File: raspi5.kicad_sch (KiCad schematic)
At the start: 6 parts, among them J1 GPIO, J3 68711614522, U1 FT24C256A

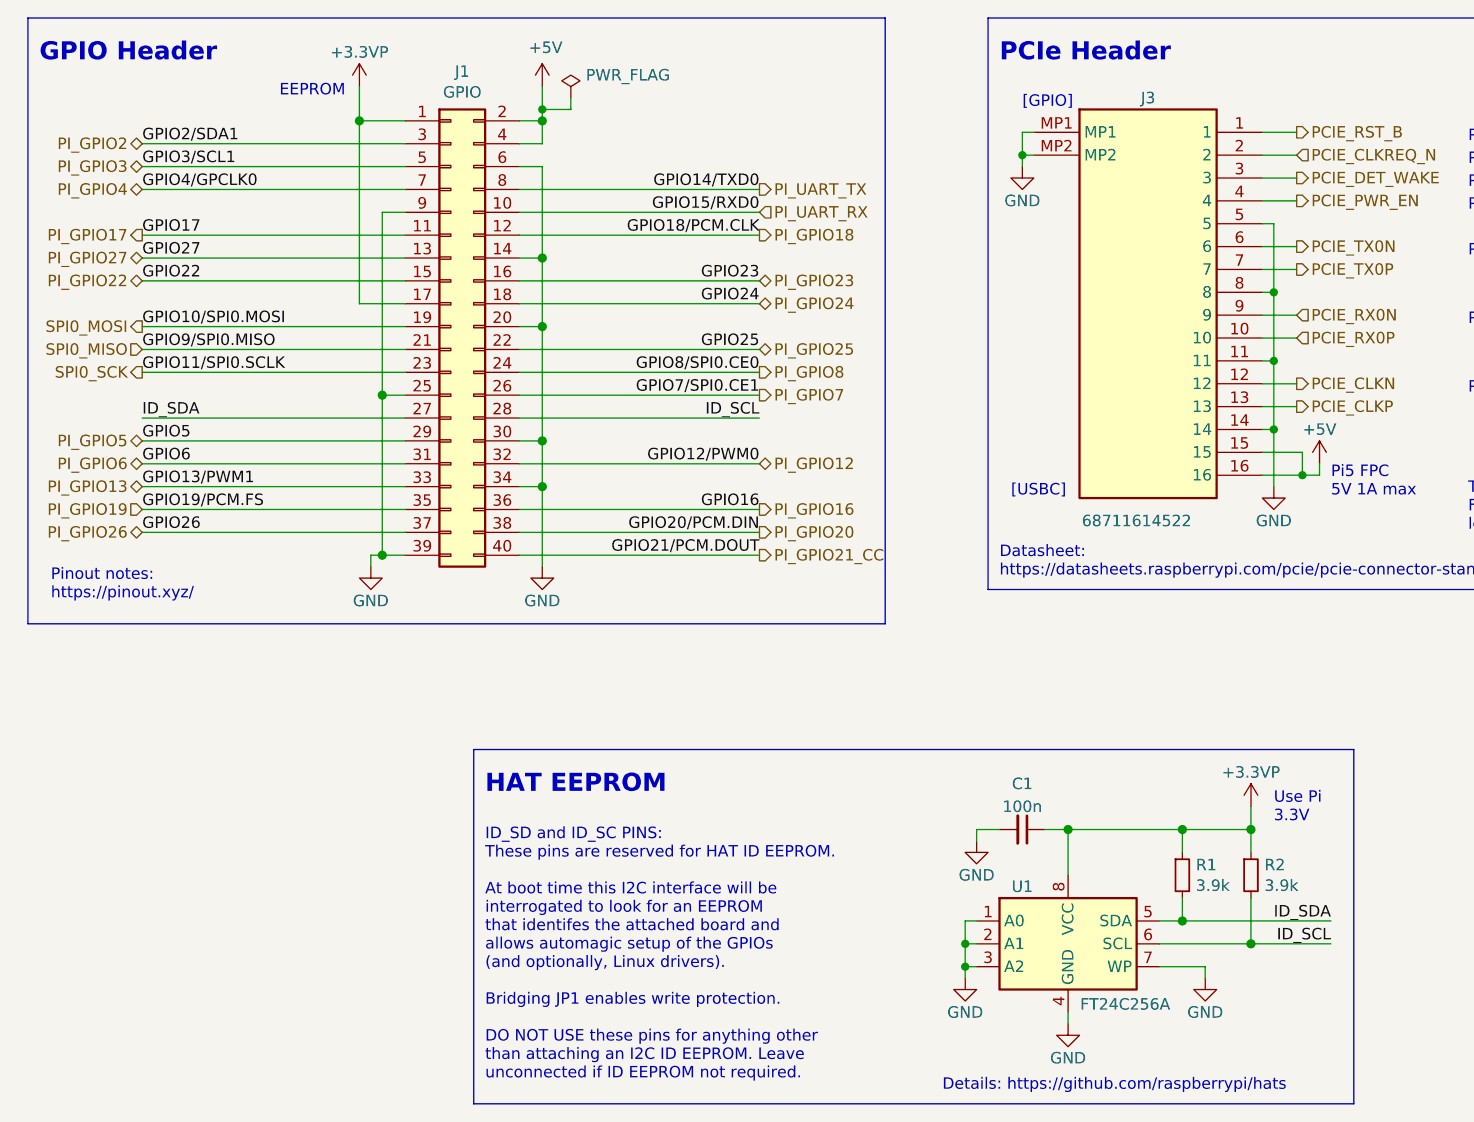
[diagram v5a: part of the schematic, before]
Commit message: Ordered boards from JLCPCB for V1
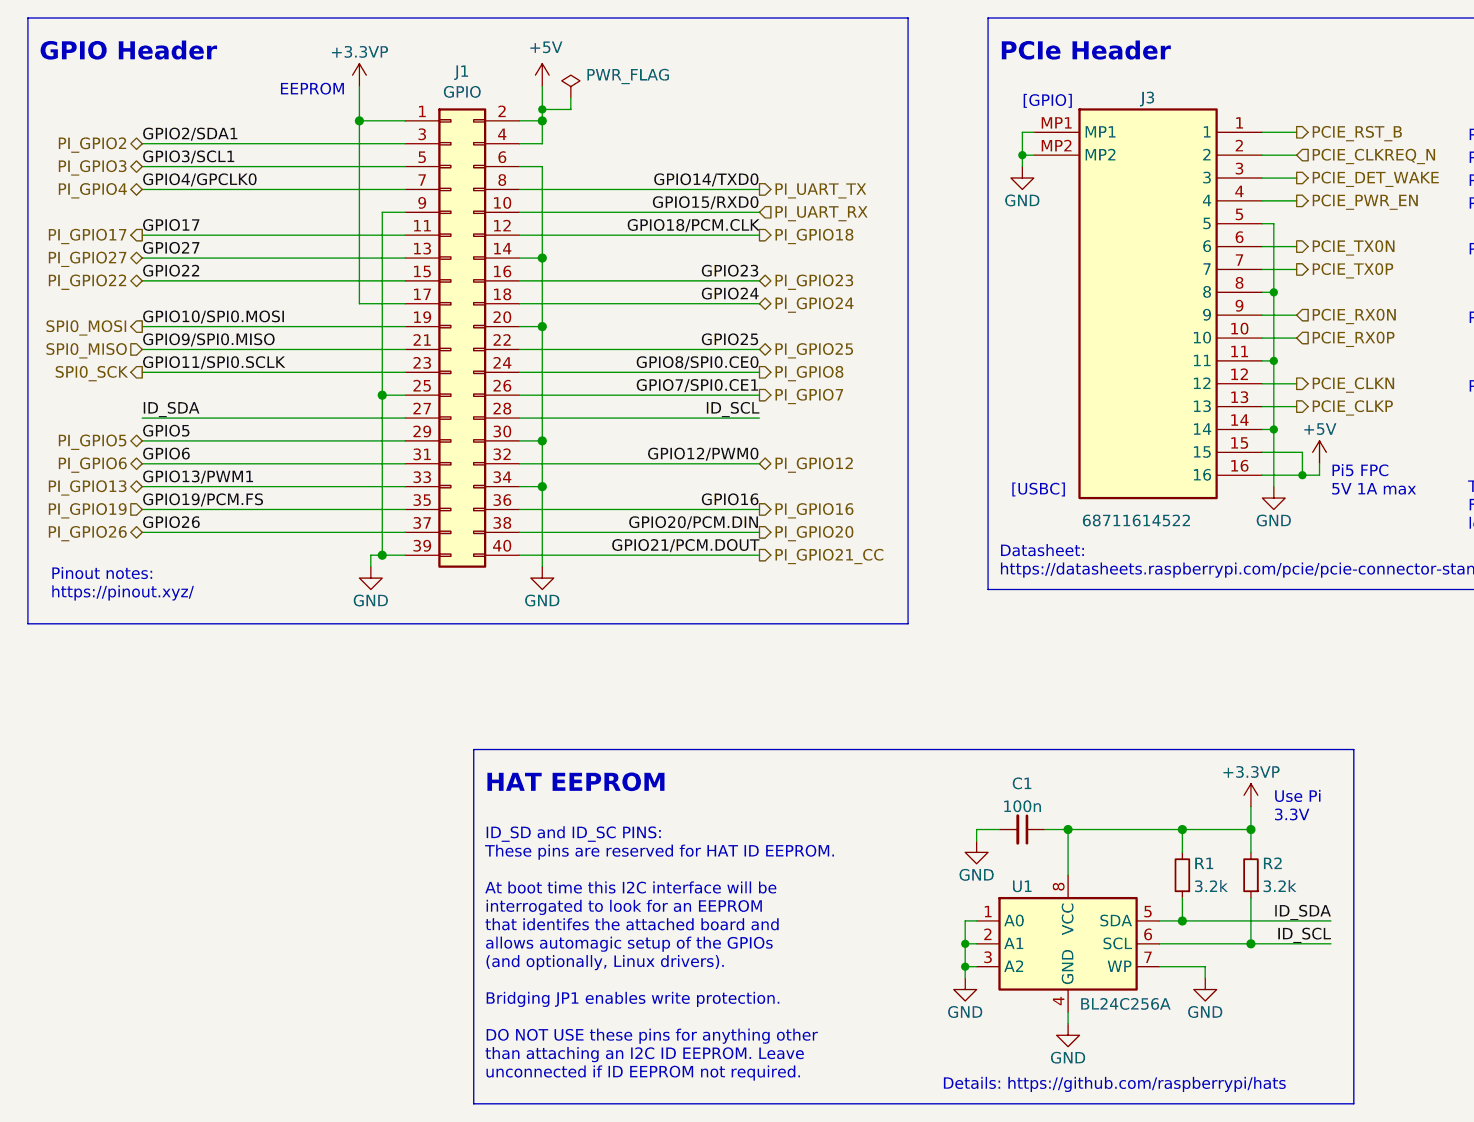
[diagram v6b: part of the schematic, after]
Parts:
- C1: footprint Capacitor_SMD:C_0402_1005Metric_Pad0.74x0.62mm_HandSolder -> Capacitor_SMD:C_0402_1005Metric
- J1: LCSC (none) -> C2977589
- J3: LCSC (none) -> C262665
- R1, R2: value 3.9k -> 3.2k; footprint Resistor_SMD:R_0402_1005Metric_Pad0.72x0.64mm_HandSolder -> Resistor_SMD:R_0402_1005Metric; LCSC (none) -> C853935
- U1: value FT24C256A -> BL24C256A; footprint Package_SO:MSOP-8_3x3mm_P0.65mm -> Package_SO:TSSOP-8_4.4x3mm_P0.65mm; LCSC C417371 -> C110276
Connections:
- net +3.3VP: now also R1.2, R2.2; no longer R1.1, R2.1
- net ID_SCL: now also R2.1; no longer R2.2
- net ID_SDA: now also R1.1; no longer R1.2

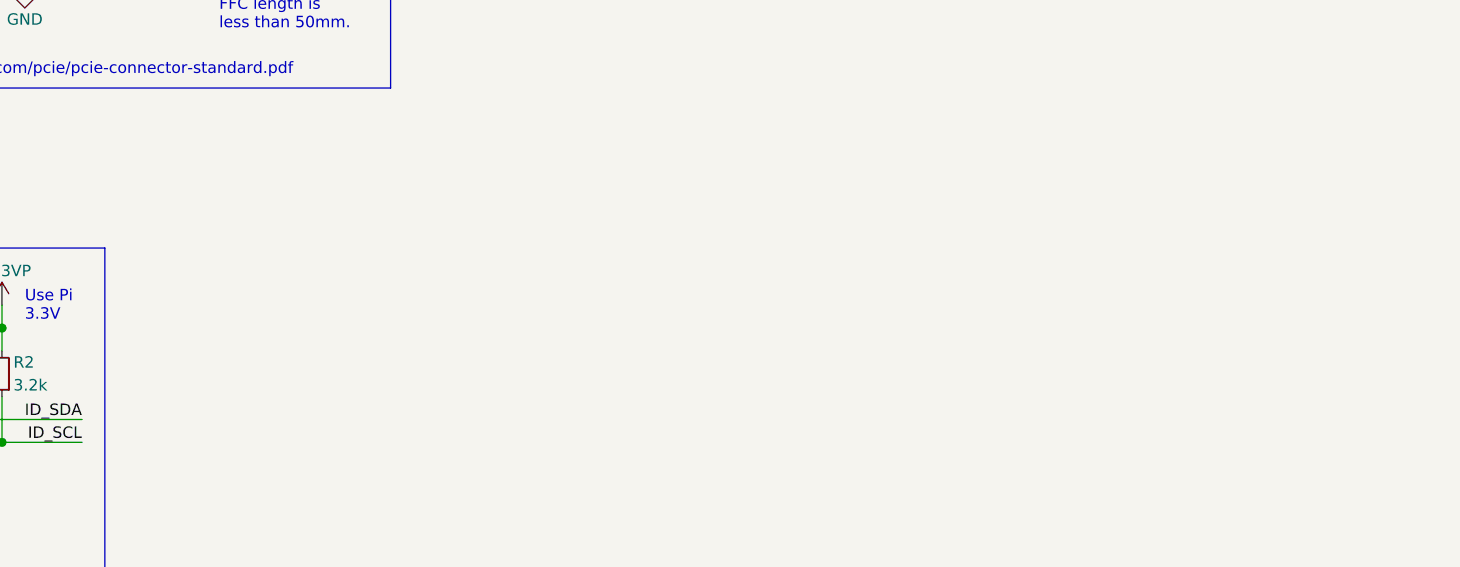
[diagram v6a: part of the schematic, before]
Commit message: Adding PCIe Example
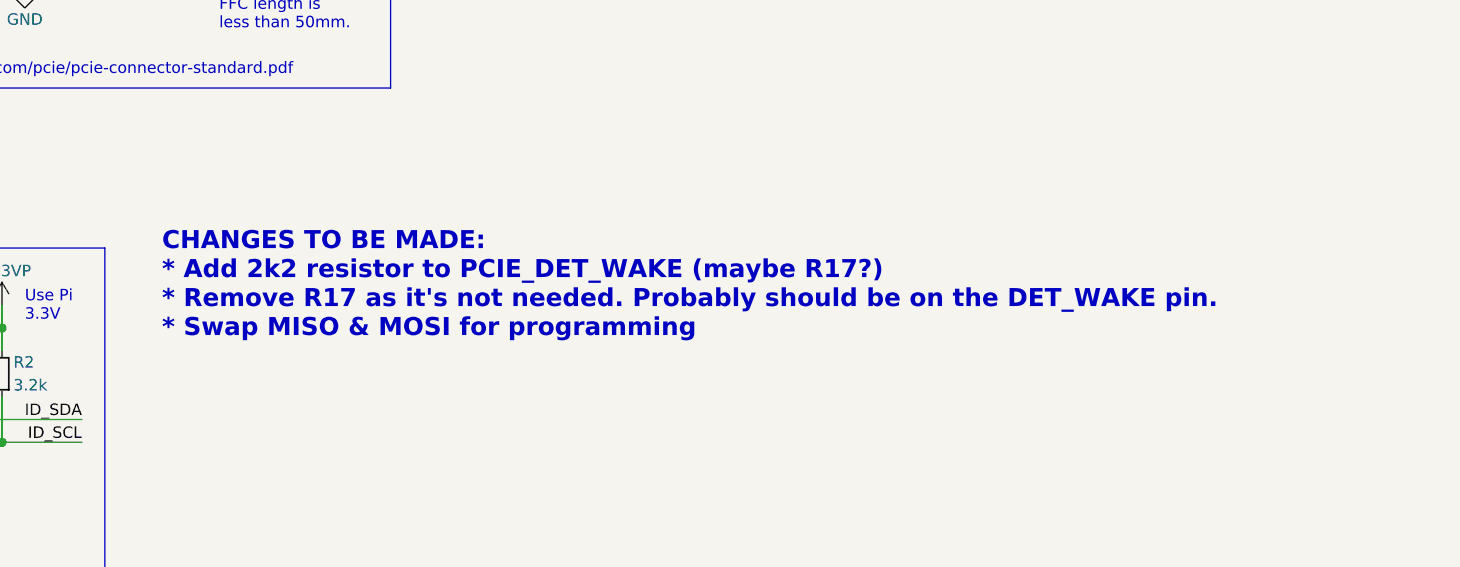
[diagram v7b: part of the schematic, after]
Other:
- note added: "CHANGES TO BE MADE: * Add 2k2 resistor to PCIE_DET_WAKE (maybe R17?) * Remove R17 as it's not needed. Probably should be on the DET_WAKE pin. * Swap MISO & MOSI for programming"
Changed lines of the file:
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@@
     (effects (font (size 1.27 1.27)) (justify left bottom))
+  )
+  (text "CHANGES TO BE MADE:\n* Add 2k2 resistor to PCIE_DET_WAKE (maybe R17?)\n* Remove R17 as it's not needed. Probably should be on the DET_WAKE pin.\n* Swap MISO & MOSI for programming"
+    (at 201.93 121.92 0)
+    (effects (font (size 2 2) (thickness 0.4) bold) (justify left bottom))
   )
   (text "EEPROM" (at 76.2 39.37 0)
